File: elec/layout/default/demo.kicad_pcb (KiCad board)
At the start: 4 copper layers, 0 parts

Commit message: [PCB] fix layout
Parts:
- added C1: 25V 1uF X5R Â±10% 0402 Multilayer Ceramic Capacitors MLCC -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, lib:C0402, F.Cu at (145.5, 108.9)
- added C10: 16V 100nF X7R Â±10% 0402 Multilayer Ceramic Capacitors MLCC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, lib:C0402, F.Cu at (145.3, 101.2)
- added C11: 16V 100nF X7R Â±10% 0402 Multilayer Ceramic Capacitors MLCC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, lib:C0402, F.Cu at (134.6, 100.2)
- added C12: 16V 100nF X7R Â±10% 0402 Multilayer Ceramic Capacitors MLCC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, lib:C0402, F.Cu at (134.7, 101.2)
- added C13: 16V 100nF X7R Â±10% 0402 Multilayer Ceramic Capacitors MLCC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, lib:C0402, F.Cu at (145.4, 105.0)
- added C14: 25V 1uF X5R Â±10% 0402 Multilayer Ceramic Capacitors MLCC -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, lib:C0402, F.Cu at (143.6, 92.0)
- added C15: 16V 100nF X7R Â±10% 0402 Multilayer Ceramic Capacitors MLCC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, lib:C0402, F.Cu at (139.9, 98.8)
- added C16: 16V 100nF X7R Â±10% 0402 Multilayer Ceramic Capacitors MLCC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, lib:C0402, F.Cu at (145.3, 100.2)
- added C17: 16V 100nF X7R Â±10% 0402 Multilayer Ceramic Capacitors MLCC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, lib:C0402, F.Cu at (142.3, 111.0)
- added C18: 25V 1uF X5R Â±10% 0402 Multilayer Ceramic Capacitors MLCC -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, lib:C0402, F.Cu at (143.3, 111.1)
- added C2: 25V 1uF X5R Â±10% 0402 Multilayer Ceramic Capacitors MLCC -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, lib:C0402, F.Cu at (148.0, 108.9)
- added C3: 6.3V 10uF X5R Â±20% 0402 Multilayer Ceramic Capacitors MLCC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, lib:C0402, B.Cu at (144.0, 107.4)
- added C4: 16V 100nF X7R Â±10% 0402 Multilayer Ceramic Capacitors MLCC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, lib:C0402, B.Cu at (143.0, 107.4)
- added C5: 10V 4.7uF X5R Â±20% 0402 Multilayer Ceramic Capacitors MLCC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, lib:C0402, B.Cu at (142.0, 107.4)
- added C6: 16V 100nF X7R Â±10% 0402 Multilayer Ceramic Capacitors MLCC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, lib:C0402, B.Cu at (141.0, 107.4)
- added C7: 50V 20pF C0G Â±5% 0402 Multilayer Ceramic Capacitors MLCC -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, lib:C0402, F.Cu at (135.9, 112.2)
- added C8: 50V 20pF C0G Â±5% 0402 Multilayer Ceramic Capacitors MLCC -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, lib:C0402, F.Cu at (141.2, 113.0)
- added C9: 16V 100nF X7R Â±10% 0402 Multilayer Ceramic Capacitors MLCC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, lib:C0402, F.Cu at (141.2, 111.0)
- added R1: 62.5mW Thick Film Resistors 50V Â±100ppm/â Â±1% 5.1kÎ© 04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, lib:R0402, F.Cu at (145.3, 106.0)
- added R2: 62.5mW Thick Film Resistors 50V Â±100ppm/â Â±1% 5.1kÎ© 04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, lib:R0402, F.Cu at (145.3, 102.2)
- added R3: 62.5mW Thick Film Resistors 50V Â±100ppm/â Â±1% 10kÎ© 040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, lib:R0402, F.Cu at (134.6, 105.0)
- added R4: 62.5mW Thick Film Resistors 50V Â±100ppm/â Â±1% 10kÎ© 040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, lib:R0402, F.Cu at (136.6, 99.1)
- added R5: 62.5mW Thick Film Resistors 50V Â±100ppm/â Â±1% 1kÎ© 0402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, lib:R0402, F.Cu at (139.7, 109.9)
- added R6: 62.5mW Thick Film Resistors 50V Â±100ppm/â Â±1% 27Î© 0402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, lib:R0402, F.Cu at (143.6, 98.1)
- added R7: 62.5mW Thick Film Resistors 50V Â±100ppm/â Â±1% 27Î© 0402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, lib:R0402, F.Cu at (143.6, 99.1)
- added U1: ?, lib:USB-C-SMD_KH-TYPE-C-16P, F.Cu at (150.0, 102.7)
- added U2: ?, lib:SOT-23-5_RIT, F.Cu at (146.8, 111.5)
- added U3: ?, lib:MAX30102EFDT, B.Cu at (142.4, 102.5)
- added U4: ?, lib:LQFN-56_L7.0-W7.0-P0.4-EP, F.Cu at (139.9, 104.0)
- added U5: KMR211NGLFS (Tactile Switches), lib:KMR211NGLFS, F.Cu at (147.2, 93.8)
- added U6: ?, lib:OSC-SMD_4P-L3.2-W2.5-BL, F.Cu at (138.5, 112.2)
- added U7: ?, lib:SOIC-8_L5.3-W5.3-P1.27-LS8.0-BL, F.Cu at (140.0, 95.1)
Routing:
- added copper zone on B.Cu, net usb_connector-vcc
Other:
- board outline added: 25 x 25 mm

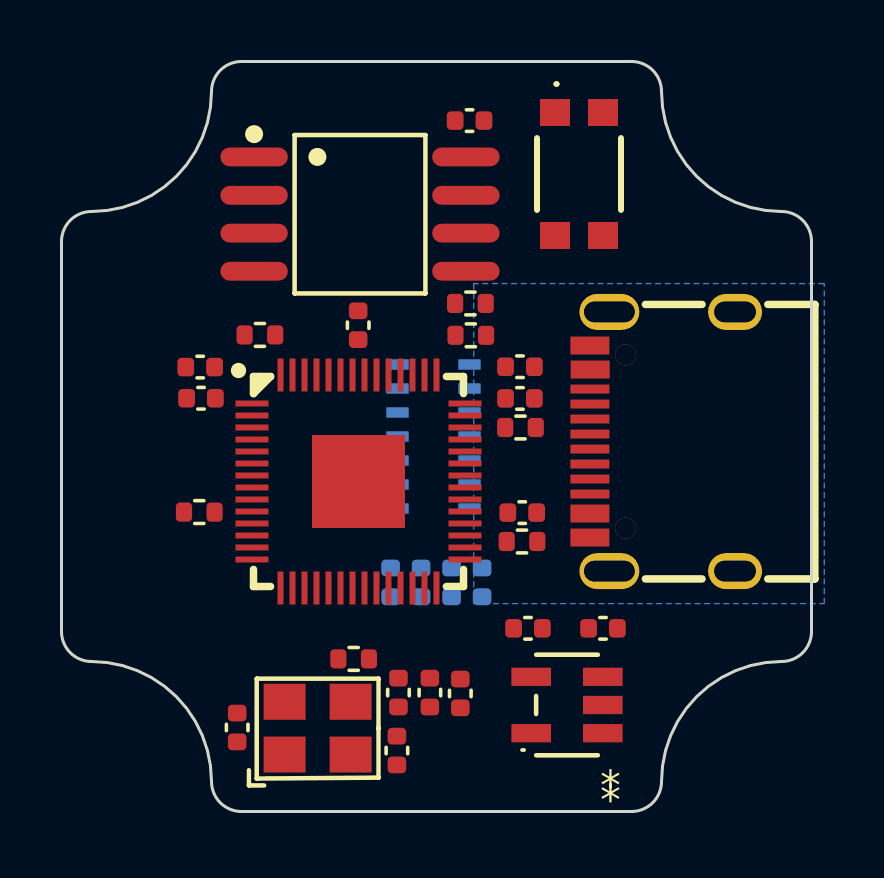
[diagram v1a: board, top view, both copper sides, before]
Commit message: [PCB] add temp
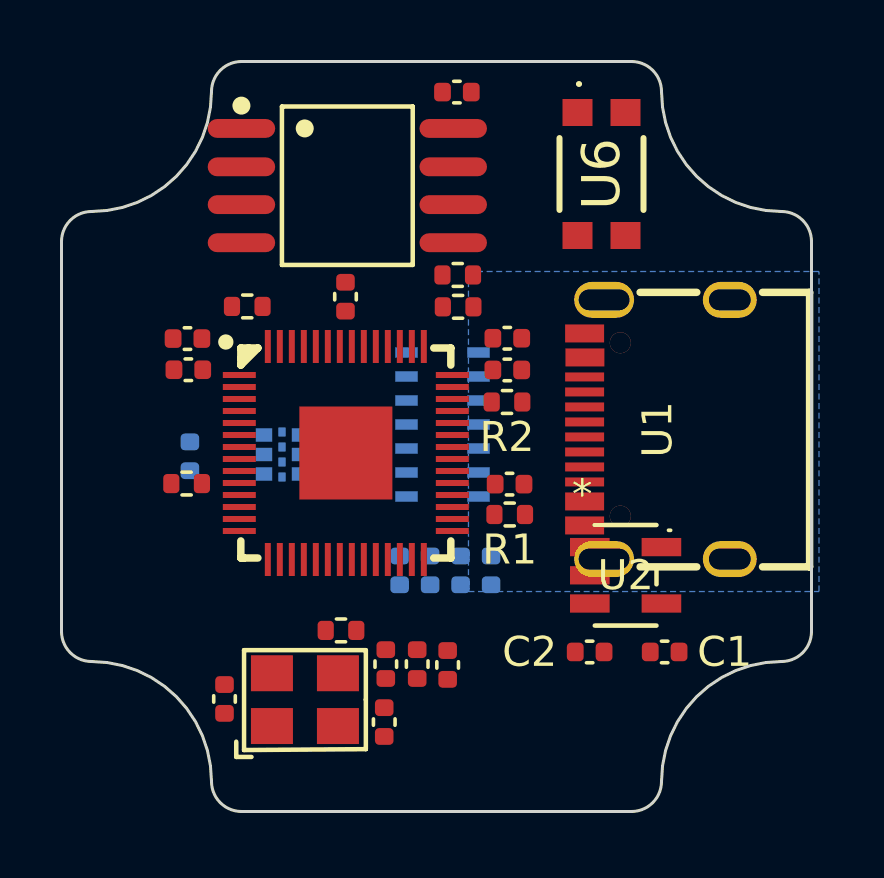
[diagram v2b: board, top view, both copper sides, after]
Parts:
- added C19: 25V 1uF X5R Â±10% 0402 Multilayer Ceramic Capacitors MLCC -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, lib:C0402, F.Cu at (142.9, 110.1)
- added U8: ?, lib:SOIC-8_L5.3-W5.3-P1.27-LS8.0-BL, F.Cu at (139.5, 94.1)
- C14, C18: value 25V 1uF X5R Â±10% 0402 Multilayer Ceramic Capacitors MLCC - SMD/SMT ROHS -> 16V 100nF X7R Â±10% 0402 Multilayer Ceramic Capacitors MLCC - SMD/SMT ROHS
- C15: value 16V 100nF X7R Â±10% 0402 Multilayer Ceramic Capacitors MLCC - SMD/SMT ROHS -> 25V 1uF X5R Â±10% 0402 Multilayer Ceramic Capacitors MLCC - SMD/SMT ROHS
- C7: value 50V 20pF C0G Â±5% 0402 Multilayer Ceramic Capacitors MLCC - SMD/SMT ROHS -> 16V 100nF X7R Â±10% 0402 Multilayer Ceramic Capacitors MLCC - SMD/SMT ROHS; moved to B.Cu
- C9: value 16V 100nF X7R Â±10% 0402 Multilayer Ceramic Capacitors MLCC - SMD/SMT ROHS -> 50V 20pF C0G Â±5% 0402 Multilayer Ceramic Capacitors MLCC - SMD/SMT ROHS
- U4: footprint lib:LQFN-56_L7.0-W7.0-P0.4-EP -> lib:MAX30208CLBT; moved to B.Cu
- U5: value KMR211NGLFS (Tactile Switches) -> ?; footprint lib:KMR211NGLFS -> lib:LQFN-56_L7.0-W7.0-P0.4-EP
- U6: value ? -> KMR211NGLFS (Tactile Switches); footprint lib:OSC-SMD_4P-L3.2-W2.5-BL -> lib:KMR211NGLFS
- U7: footprint lib:SOIC-8_L5.3-W5.3-P1.27-LS8.0-BL -> lib:OSC-SMD_4P-L3.2-W2.5-BL
- moved U6 20.8 mm to (148.0, 93.8), turned to 90 degrees
- moved U7 16.3 mm to (138.1, 111.3), turned to 0 degrees
- moved C14 12.2 mm to (144.9, 104.1), turned to 0 degrees
- moved U5 12.1 mm to (139.5, 103.0), turned to 0 degrees
- moved C13 12.1 mm to (134.2, 100.3), turned to 180 degrees
- moved C17 12.1 mm to (144.9, 99.2), turned to 0 degrees
- moved C11 10.2 mm to (144.9, 100.3), turned to 0 degrees
- moved C10 9.92 mm to (140.8, 110.1), turned to -90 degrees
- moved C7 9.17 mm to (134.3, 103.2)
- moved C15 8.44 mm to (143.2, 91.0), turned to 180 degrees
- moved C16 6.27 mm to (139.5, 97.8), turned to 90 degrees
- moved C8 6.00 mm to (135.4, 111.2), turned to 90 degrees
- moved U2 4.74 mm to (148.8, 107.1), turned to 0 degrees
- moved C1 4.62 mm to (150.1, 109.7), turned to 180 degrees
- moved U4 2.70 mm to (137.3, 103.1)
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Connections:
- C15 pad 1: microcontroller.rp2040.micro-vcc -> power_supply-vcc
- C7 pad 1: xin -> temperature_sensor.sensor-vcc
- C7 pad 2: usb_connector-gnd-1 -> sensor-gnd
- C8 pad 1: out -> xin
- C9 pad 1: power_supply-vcc -> out
- U4 pad 1: power_supply-vcc -> temperature_sensor.sensor-vcc
- U4 pad 10: power_supply-vcc -> temperature_sensor.sensor-io-1
- U4 pad 2: gpio0 -> temperature_sensor.sensor-vcc
- U4 pad 3: gpio1 -> temperature_sensor.sensor-vcc
- U4 pad 4: gpio2 -> sensor-gnd
- U4 pad 5: gpio3 -> sensor-gnd
- U4 pad 6: tx -> sensor-gnd
- U4 pad 7: rx -> temperature_sensor.sensor-io
- U4 pad 8: gpio6 -> sda
- U4 pad 9: gpio7 -> scl
- U5 pad 1: usb_connector-gnd-1 -> power_supply-vcc
- U5 pad 2: microcontroller.rp2040-cs-1 -> gpio0
- U5 pad 3: microcontroller.rp2040-cs-1 -> gpio1
- U5 pad 4: usb_connector-gnd-1 -> gpio2
- U6 pad 1: xin -> usb_connector-gnd-1
- U6 pad 2: usb_connector-gnd-1 -> microcontroller.rp2040-cs-1
- U6 pad 3: out -> microcontroller.rp2040-cs-1
- U7 pad 1: microcontroller.rp2040-cs-1 -> xin
- U7 pad 2: io1 -> usb_connector-gnd-1
- U7 pad 3: io2 -> out

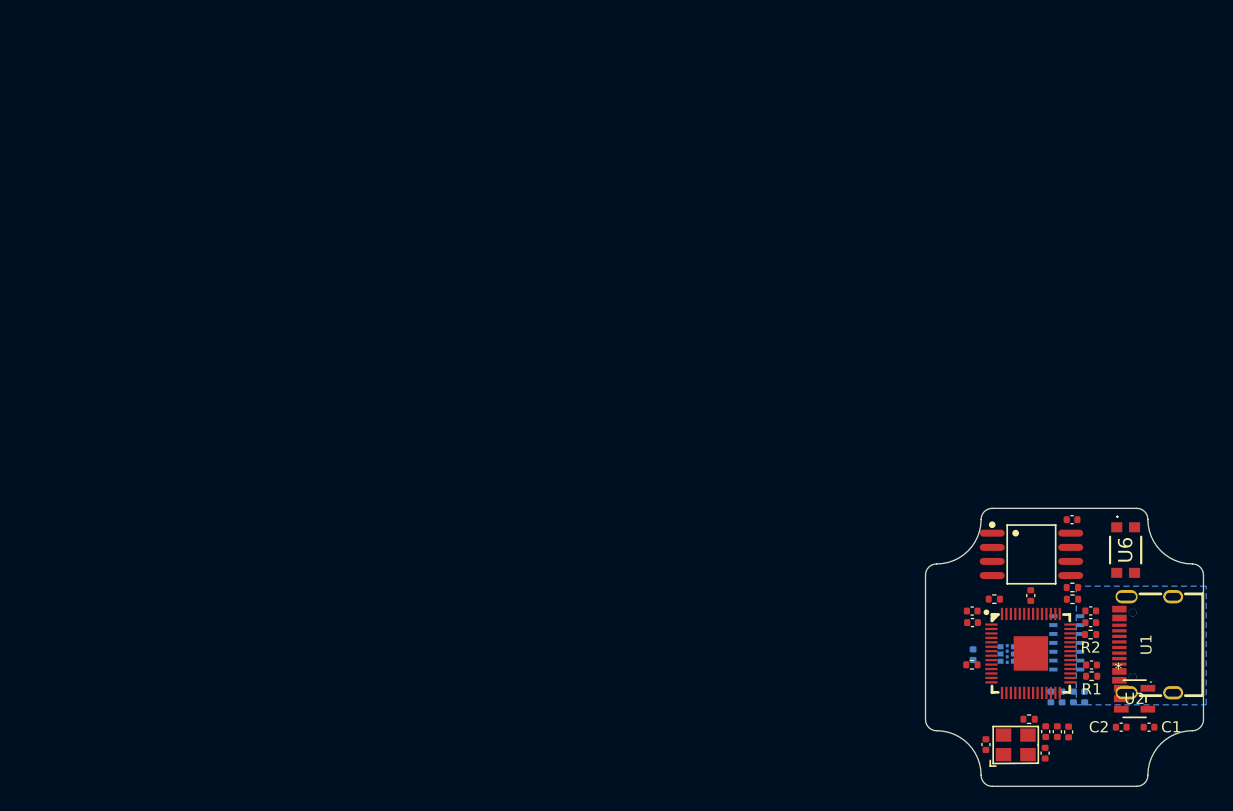
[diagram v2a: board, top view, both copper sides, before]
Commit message: [ELEC] messed up layout
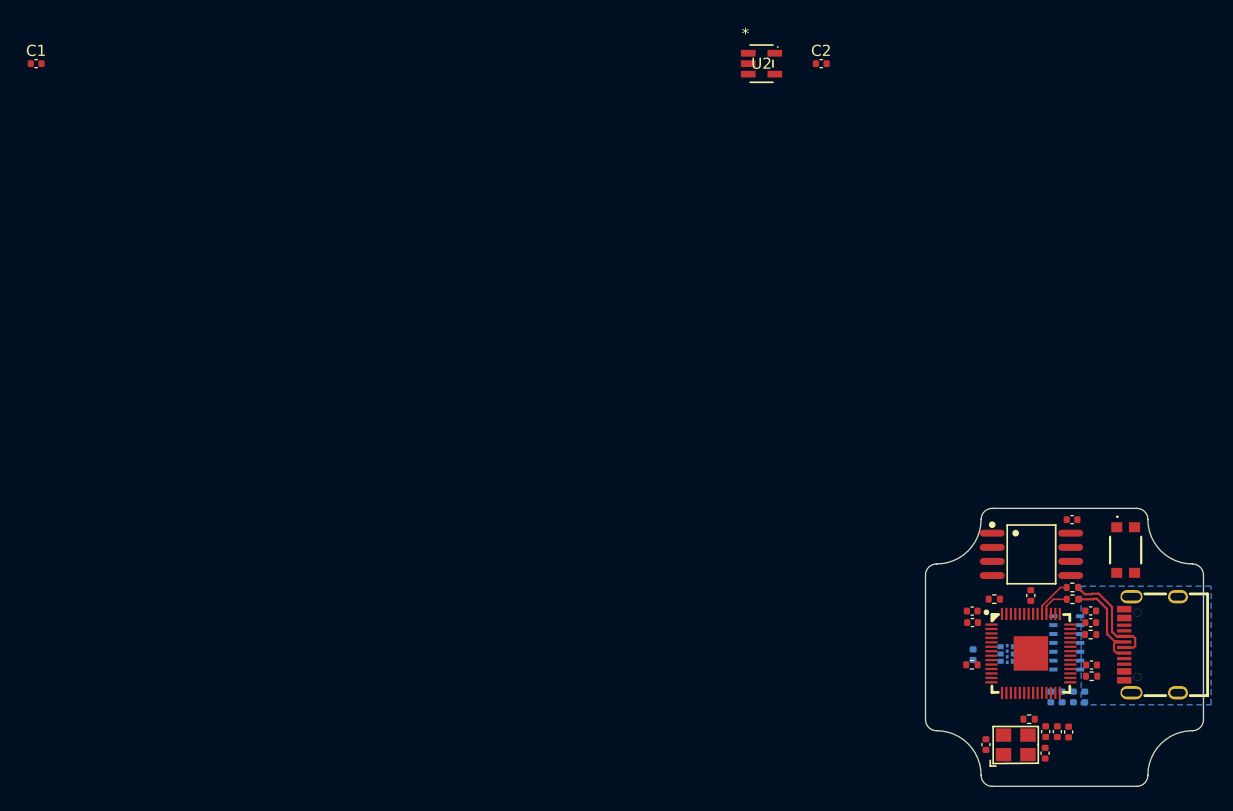
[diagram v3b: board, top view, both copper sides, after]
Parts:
- moved C1 116.5 mm to (50.0, 50.0), turned to 0 degrees
- moved U2 66.3 mm to (115.3, 50.0)
- moved C2 65.5 mm to (120.6, 50.0)
- moved U1 0.43 mm to (150.3, 102.3)
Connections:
- net dm renamed usb_N
- net dp renamed usb_P
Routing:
- net usb_P: track 0.00 -> 10.1 mm
- net usb_N: track 0.00 -> 8.96 mm
- net usb_dp: track 0.00 -> 3.63 mm
- net usb_dm: track 0.00 -> 2.79 mm
